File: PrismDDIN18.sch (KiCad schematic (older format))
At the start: 89 parts, among them CON1 BARREL_JACK, IC1 LM2596T-5, J1 Conn_01x03, M1 IN-18, M10 IN-18, Q2 2N7000, Q3 2N7000, Q4 2N7000, Q5 2N7000, Q6 IRF540N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

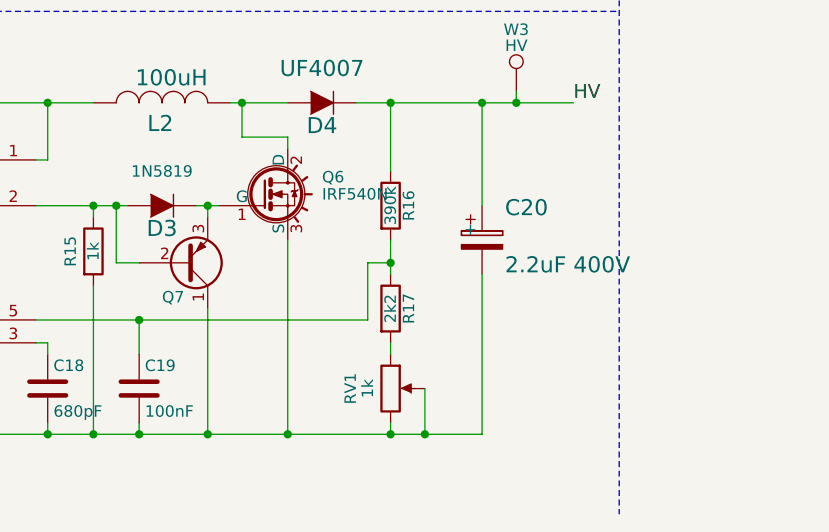
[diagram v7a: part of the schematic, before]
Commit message: Update component values
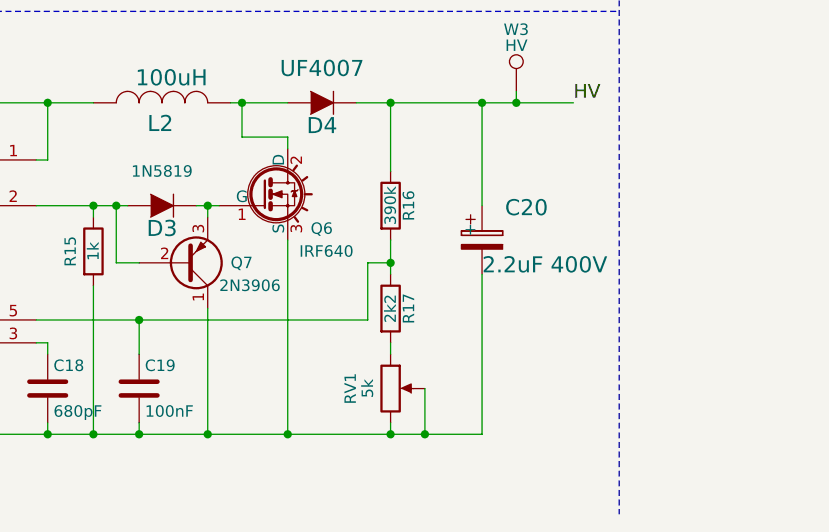
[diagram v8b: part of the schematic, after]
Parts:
- Q6: value IRF540N -> IRF640
- Q7: value Q_PNP_BCE -> 2N3906
- RV1: value 1k -> 5k
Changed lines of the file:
@@
 P 10450 10650
 F 0 "RV1" V 10275 10650 50  0000 C CNN
-F 1 "1k" V 10350 10650 50  0000 C CNN
+F 1 "5k" V 10350 10650 50  0000 C CNN
 F 2 "NixieClockMaster:Potentiometer_Trimmer_Bourns_3296X" H 10450 10650 50  0001 C CNN
 F 3 "" H 10450 10650 50  0000 C CNN
@@
 P 10850 10000
 F 0 "C20" H 10950 10100 70  0000 L BNN
-F 1 "2.2uF 400V" H 10950 9850 70  0000 L BNN
+F 1 "2.2uF 400V" H 10850 9850 70  0000 L BNN
 F 2 "NixieClockMaster:C_Radial_D6.3_L11.2_P2.5" H 10840 9790 70  0001 L TNN
 F 3 "" H 10850 10000 60  0001 C CNN
@@
 U 1 1 5937A70F
 P 9550 10100
-F 0 "Q7" H 9450 10250 50  0000 L CNN
-F 1 "Q_PNP_BCE" H 9750 10050 50  0001 L CNN
+F 0 "Q7" H 9750 10100 50  0000 L CNN
+F 1 "2N3906" H 9700 10200 50  0000 L CNN
 F 2 "NixieClockMaster:2N7000_TO92" H 9750 10200 50  0001 C CNN
 F 3 "" H 9550 10100 50  0000 C CNN
@@
 U 1 1 5937F7A9
 P 9900 9800
-F 0 "Q6" H 10150 9875 50  0000 L CNN
-F 1 "IRF540N" H 10150 9800 50  0000 L CNN
+F 0 "Q6" H 10100 9650 50  0000 L CNN
+F 1 "IRF640" H 10050 9550 50  0000 L CNN
 F 2 "NixieClockMaster:TO-220-3_H" H 10150 9725 50  0001 L CIN
 F 3 "" H 9900 9800 50  0000 L CNN
